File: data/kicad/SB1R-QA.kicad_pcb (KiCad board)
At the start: 4 copper layers, 230 x 228 mm, 5 parts

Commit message: Damping resistors 680 ohm, results, docs and regression for SB1R-Q
- RD1/RD2 value 680 ohm (minimax first gate over Cself 50-200 pF with the
  real AB1T input): 5.1-5.5 us aligned, 7.1-7.5 us at the worst real leak
  (10 mV); gated noise +4 % at 6 us, < 2 % from 20 us. Firmware rule: keep
  BLANK open through turn-off unless the leak exceeds amplifier headroom.
- QB leak after moving its terminals to r23 and re-tuning B (9/9/9/20/6):
  0.07 / 0.59 / 6.0 / 10.3 mV (was 0.005 / 0.85 / 4.4 / 11.0 mV).
- Regenerated SB1R-QA/QB Gerbers and KiCad files, seeds and results;
  sbq_damping.json replaced by sbq_damping2.json; figures SBQ_DAMPING2,
  RX_PLATFORM_QUAD and LEVELS_SCHEMATIC redrawn.
- DESIGN_STATE, CORRECTIONS (5 rows), ASSUMPTIONS (row 14, new row 21),
  OPEN_ITEMS (1 and 12), check counts, stale P01/P02/C04 prompts.
- regress.py: 47 geometry checks, damping fitted, first gate and noise.

Co-Authored-By: Claude Opus 5.5 <noreply@anthropic.com>
Claude-Session: https://claude.ai/code/session_01SK9nuqTzvCJwnmscD6XRZs
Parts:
- added RD1: 680R 0.1% thin film 0805, non-magnetic terminations preferr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, Resistor_SMD:R_0805_2012Metric, F.Cu at (150.0, 87.0)
- added RD2: 680R 0.1% thin film 0805, non-magnetic terminations preferr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, Resistor_SMD:R_0805_2012Metric, F.Cu at (133.9, 103.9)
- added T1: , SB1R:TRANSFER_PAD, F.Cu at (135.8, 101.9)
- added T2: , SB1R:TRANSFER_PAD, F.Cu at (131.9, 105.8)
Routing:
- net QA_COIL: track 16989.1 -> 16995.2 mm
- net QB_COIL: track 0.00 -> 3.64 mm
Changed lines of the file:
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@@
   (net 0 "")
   (net 1 "QA_COIL")
+  (net 2 "QB_COIL")
+  (footprint "SB1R:TRANSFER_PAD" (layer "F.Cu") (at 135.812 101.898) (property "Reference" "T1" (at 0 -2) (layer "F.SilkS")) (pad "1" thru_hole circle (at 0 0) (size 1.6 1.6) (drill 0.8) (layers "*.Cu" "*.Mask") (net 2 "QB_COIL")))
+  (footprint "SB1R:TRANSFER_PAD" (layer "F.Cu") (at 131.898 105.812) (property "Reference" "T2" (at 0 -2) (layer "F.SilkS")) (pad "1" thru_hole circle (at 0 0) (size 1.6 1.6) (drill 0.8) (layers "*.Cu" "*.Mask") (net 2 "QB_COIL")))
+  (footprint "Resistor_SMD:R_0805_2012Metric" (layer "F.Cu") (at 150.000 87.000 180.000) (property "Reference" "RD1" (at 0 -1.6) (layer "F.SilkS")) (property "Value" "680R 0.1% thin film 0805, non-magnetic terminations preferred (unverified)" (at 0 1.6) (layer "F.Fab")) (pad "1" smd roundrect (at -0.95 0 180.000) (size 1.0 1.3) (layers "F.Cu" "F.Paste" "F.Mask") (roundrect_rratio 0.25) (net 1 "QA_COIL")) (pad "2" smd roundrect (at 0.95 0 180.000) (size 1.0 1.3) (layers "F.Cu" "F.Paste" "F.Mask") (roundrect_rratio 0.25) (net 1 "QA_COIL")))
+  (footprint "Resistor_SMD:R_0805_2012Metric" (layer "F.Cu") (at 133.855 103.855 -135.000) (property "Reference" "RD2" (at 0 -1.6) (layer "F.SilkS")) (property "Value" "680R 0.1% thin film 0805, non-magnetic terminations preferred (unverified)" (at 0 1.6) (layer "F.Fab")) (pad "1" smd roundrect (at -0.95 0 -135.000) (size 1.0 1.3) (layers "F.Cu" "F.Paste" "F.Mask") (roundrect_rratio 0.25) (net 2 "QB_COIL")) (pad "2" smd roundrect (at 0.95 0 -135.000) (size 1.0 1.3) (layers "F.Cu" "F.Paste" "F.Mask") (roundrect_rratio 0.25) (net 2 "QB_COIL")))
+  (segment (start 154.0000 87.0000) (end 150.9500 87.0000) (width 0.4) (layer "F.Cu") (net 1))
+  (segment (start 149.0500 87.0000) (end 146.0000 87.0000) (width 0.4) (layer "F.Cu") (net 1))
+  (segment (start 135.8117 101.8977) (end 134.5265 103.1830) (width 0.4) (layer "F.Cu") (net 2))
+  (segment (start 133.1830 104.5265) (end 131.8977 105.8117) (width 0.4) (layer "F.Cu") (net 2))
   (footprint "SB1R:LEAD_PAD" (layer "F.Cu") (at 154.000 87.000) (property "Reference" "P1" (at 0 -2) (layer "F.SilkS")) (pad "1" thru_hole circle (at 0 0) (size 1.6 1.6) (drill 0.8) (layers "*.Cu" "*.Mask") (net 1 "QA_COIL")))
   (footprint "SB1R:LEAD_PAD" (layer "F.Cu") (at 146.000 87.000) (property "Reference" "P2" (at 0 -2) (layer "F.SilkS")) (pad "1" thru_hole circle (at 0 0) (size 1.6 1.6) (drill 0.8) (layers "*.Cu" "*.Mask") (net 1 "QA_COIL")))

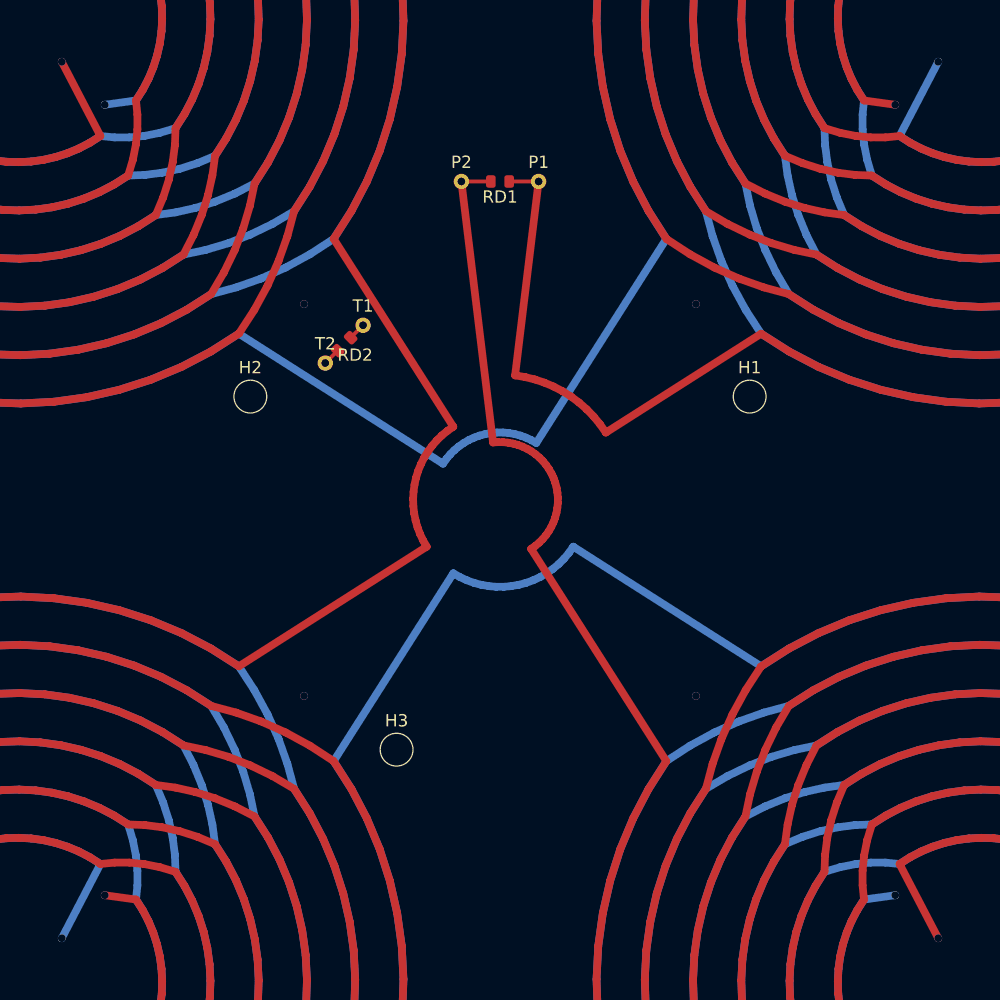
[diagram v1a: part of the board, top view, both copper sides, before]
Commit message: Step 2: CB1D options, SB1R via drill, TXJ1 pads, fab-floor rules, finishes (KiCad 9: 5 boards, 0 errors / 0 unconnected)
- SB1R: via drill 0.4 mm (was 0.8 = no annular ring in the KiCad files and the PTH drill files); QB transfer nets QB_T1/QB_T2; Gerbers SB1R_QA_v2 / SB1R_QB_v2, old marked superseded; sbq sims unchanged (0 numbers moved)
- TXJ1: AWG12 pads 3.8 mm (edge distance 0.6 mm); Gerbers TXJ1_v2
- CB1D: RJB10 0R fitted on JB.10, RJ5/RJ6 DNP grounds for JTR.5/.6 (61 parts, 44/44 nets); Gerbers CB1D_B2; wiring alias JB10_VCM
- dru_gen: conservative Advanced Circuits / TTM floor (UNVERIFIED), SB1R keys; no ENIG near the coil/receivers (immersion silver / HASL); docs/design/FAB_RULES.md
- make kicad-drc covers CB1D, LB1, TXJ1, SB1R-QA/QB; regress 42 pass; CORRECTIONS, DESIGN_STATE, OPEN_ITEMS 23/25-27, ASSUMPTIONS 31

Co-Authored-By: Claude Sonnet 5.5 <noreply@anthropic.com>
Claude-Session: https://claude.ai/code/session_01T7iU5pGiBfkKRBbe2JcTJx
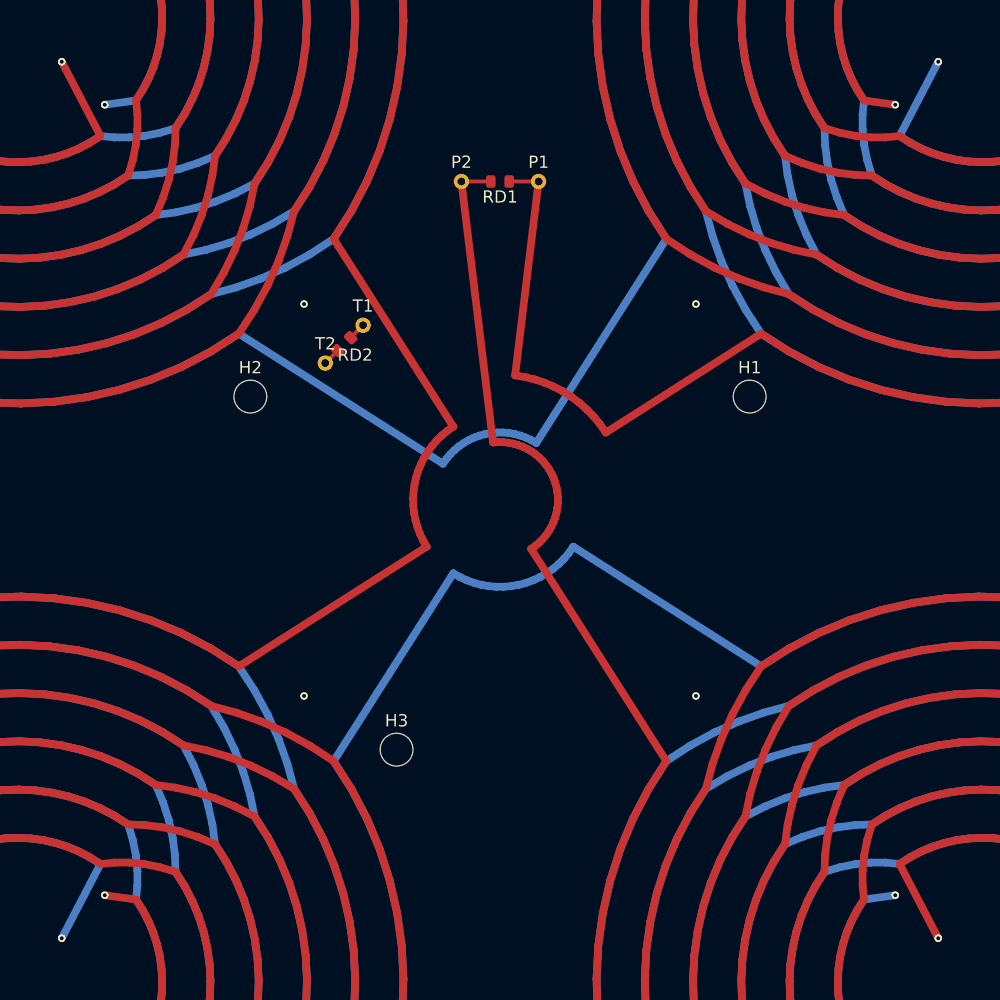
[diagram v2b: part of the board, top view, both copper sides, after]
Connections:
- RD2 pad 1: QB_COIL -> QB_T1
- RD2 pad 2: QB_COIL -> QB_T2
- T1 pad 1: QB_COIL -> QB_T1
- T2 pad 1: QB_COIL -> QB_T2
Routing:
- net QB_COIL: track 3.64 -> 0.00 mm
- net QB_T2: track 0.00 -> 1.82 mm
- net QB_T1: track 0.00 -> 1.82 mm
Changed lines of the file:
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@@
   (paper "A3")
   (layers (0 "F.Cu" signal) (1 "In1.Cu" signal) (2 "In2.Cu" signal) (31 "B.Cu" signal) (34 "B.Paste" user) (35 "F.Paste" user) (36 "B.SilkS" user "B.Silkscreen") (37 "F.SilkS" user "F.Silkscreen") (38 "B.Mask" user) (39 "F.Mask" user) (40 "Dwgs.User" user "User.Drawings") (41 "Cmts.User" user "User.Comments") (44 "Edge.Cuts" user) (47 "F.CrtYd" user "F.Courtyard") (49 "F.Fab" user))
-  (setup (pad_to_mask_clearance 0.05) (stackup (layer "F.Cu" (type "copper") (thickness 0.035)) (layer "dielectric 1" (type "prepreg") (thickness 0.15)) (layer "In1.Cu" (type "copper") (thickness 0.035)) (layer "dielectric 2" (type "core") (thickness 0.34)) (layer "In2.Cu" (type "copper") (thickness 0.035)) (layer "dielectric 3" (type "prepreg") (thickness 0.15)) (layer "B.Cu" (type "copper") (thickness 0.035)) (copper_finish "ENIG")))
+  (setup (pad_to_mask_clearance 0.05) (stackup (layer "F.Cu" (type "copper") (thickness 0.035)) (layer "dielectric 1" (type "prepreg") (thickness 0.15)) (layer "In1.Cu" (type "copper") (thickness 0.035)) (layer "dielectric 2" (type "core") (thickness 0.34)) (layer "In2.Cu" (type "copper") (thickness 0.035)) (layer "dielectric 3" (type "prepreg") (thickness 0.15)) (layer "B.Cu" (type "copper") (thickness 0.035)) (copper_finish "Immersion silver")))
   (net 0 "")
   (net 1 "QA_COIL")
-  (net 2 "QB_COIL")
-  (footprint "SB1R:TRANSFER_PAD" (layer "F.Cu") (at 135.812 101.898) (property "Reference" "T1" (at 0 -2) (layer "F.SilkS")) (pad "1" thru_hole circle (at 0 0) (size 1.6 1.6) (drill 0.8) (layers "*.Cu" "*.Mask") (net 2 "QB_COIL")))
-  (footprint "SB1R:TRANSFER_PAD" (layer "F.Cu") (at 131.898 105.812) (property "Reference" "T2" (at 0 -2) (layer "F.SilkS")) (pad "1" thru_hole circle (at 0 0) (size 1.6 1.6) (drill 0.8) (layers "*.Cu" "*.Mask") (net 2 "QB_COIL")))
+  (net 2 "QB_T1")
+  (net 3 "QB_T2")
+  (footprint "SB1R:TRANSFER_PAD" (layer "F.Cu") (at 135.812 101.898) (property "Reference" "T1" (at 0 -2) (layer "F.SilkS")) (pad "1" thru_hole circle (at 0 0) (size 1.6 1.6) (drill 0.8) (layers "*.Cu" "*.Mask") (net 2 "QB_T1")))
+  (footprint "SB1R:TRANSFER_PAD" (layer "F.Cu") (at 131.898 105.812) (property "Reference" "T2" (at 0 -2) (layer "F.SilkS")) (pad "1" thru_hole circle (at 0 0) (size 1.6 1.6) (drill 0.8) (layers "*.Cu" "*.Mask") (net 3 "QB_T2")))
   (footprint "Resistor_SMD:R_0805_2012Metric" (layer "F.Cu") (at 150.000 87.000 180.000) (property "Reference" "RD1" (at 0 -1.6) (layer "F.SilkS")) (property "Value" "680R 0.1% thin film 0805, non-magnetic terminations preferred (unverified)" (at 0 1.6) (layer "F.Fab")) (pad "1" smd roundrect (at -0.95 0 180.000) (size 1.0 1.3) (layers "F.Cu" "F.Paste" "F.Mask") (roundrect_rratio 0.25) (net 1 "QA_COIL")) (pad "2" smd roundrect (at 0.95 0 180.000) (size 1.0 1.3) (layers "F.Cu" "F.Paste" "F.Mask") (roundrect_rratio 0.25) (net 1 "QA_COIL")))
-  (footprint "Resistor_SMD:R_0805_2012Metric" (layer "F.Cu") (at 133.855 103.855 -135.000) (property "Reference" "RD2" (at 0 -1.6) (layer "F.SilkS")) (property "Value" "680R 0.1% thin film 0805, non-magnetic terminations preferred (unverified)" (at 0 1.6) (layer "F.Fab")) (pad "1" smd roundrect (at -0.95 0 -135.000) (size 1.0 1.3) (layers "F.Cu" "F.Paste" "F.Mask") (roundrect_rratio 0.25) (net 2 "QB_COIL")) (pad "2" smd roundrect (at 0.95 0 -135.000) (size 1.0 1.3) (layers "F.Cu" "F.Paste" "F.Mask") (roundrect_rratio 0.25) (net 2 "QB_COIL")))
+  (footprint "Resistor_SMD:R_0805_2012Metric" (layer "F.Cu") (at 133.855 103.855 -135.000) (property "Reference" "RD2" (at 0 -1.6) (layer "F.SilkS")) (property "Value" "680R 0.1% thin film 0805, non-magnetic terminations preferred (unverified)" (at 0 1.6) (layer "F.Fab")) (pad "1" smd roundrect (at -0.95 0 -135.000) (size 1.0 1.3) (layers "F.Cu" "F.Paste" "F.Mask") (roundrect_rratio 0.25) (net 2 "QB_T1")) (pad "2" smd roundrect (at 0.95 0 -135.000) (size 1.0 1.3) (layers "F.Cu" "F.Paste" "F.Mask") (roundrect_rratio 0.25) (net 3 "QB_T2")))
   (segment (start 154.0000 87.0000) (end 150.9500 87.0000) (width 0.4) (layer "F.Cu") (net 1))
   (segment (start 149.0500 87.0000) (end 146.0000 87.0000) (width 0.4) (layer "F.Cu") (net 1))
   (segment (start 135.8117 101.8977) (end 134.5265 103.1830) (width 0.4) (layer "F.Cu") (net 2))
-  (segment (start 133.1830 104.5265) (end 131.8977 105.8117) (width 0.4) (layer "F.Cu") (net 2))
+  (segment (start 133.1830 104.5265) (end 131.8977 105.8117) (width 0.4) (layer "F.Cu") (net 3))
   (footprint "SB1R:LEAD_PAD" (layer "F.Cu") (at 154.000 87.000) (property "Reference" "P1" (at 0 -2) (layer "F.SilkS")) (pad "1" thru_hole circle (at 0 0) (size 1.6 1.6) (drill 0.8) (layers "*.Cu" "*.Mask") (net 1 "QA_COIL")))
   (footprint "SB1R:LEAD_PAD" (layer "F.Cu") (at 146.000 87.000) (property "Reference" "P2" (at 0 -2) (layer "F.SilkS")) (pad "1" thru_hole circle (at 0 0) (size 1.6 1.6) (drill 0.8) (layers "*.Cu" "*.Mask") (net 1 "QA_COIL")))
@@
   (segment (start 157.1406 125.4782) (end 157.5909 124.8350) (width 0.8) (layer "B.Cu") (net 1))
   (segment (start 157.5909 124.8350) (end 177.0569 137.2339) (width 0.8) (layer "B.Cu") (net 1))
-  (via (at 190.9490 79.0510) (size 0.8) (drill 0.8) (layers "F.Cu" "B.Cu") (net 1))
-  (via (at 170.3015 99.6985) (size 0.8) (drill 0.8) (layers "F.Cu" "B.Cu") (net 1))
-  (via (at 195.4038 74.5962) (size 0.8) (drill 0.8) (layers "F.Cu" "B.Cu") (net 1))
-  (via (at 109.0510 79.0510) (size 0.8) (drill 0.8) (layers "F.Cu" "B.Cu") (net 1))
-  (via (at 129.6985 99.6985) (size 0.8) (drill 0.8) (layers "F.Cu" "B.Cu") (net 1))
-  (via (at 104.5962 74.5962) (size 0.8) (drill 0.8) (layers "F.Cu" "B.Cu") (net 1))
-  (via (at 109.0510 160.9490) (size 0.8) (drill 0.8) (layers "F.Cu" "B.Cu") (net 1))
-  (via (at 129.6985 140.3015) (size 0.8) (drill 0.8) (layers "F.Cu" "B.Cu") (net 1))
-  (via (at 104.5962 165.4038) (size 0.8) (drill 0.8) (layers "F.Cu" "B.Cu") (net 1))
-  (via (at 190.9490 160.9490) (size 0.8) (drill 0.8) (layers "F.Cu" "B.Cu") (net 1))
-  (via (at 170.3015 140.3015) (size 0.8) (drill 0.8) (layers "F.Cu" "B.Cu") (net 1))
-  (via (at 195.4038 165.4038) (size 0.8) (drill 0.8) (layers "F.Cu" "B.Cu") (net 1))
+  (via (at 190.9490 79.0510) (size 0.8) (drill 0.4) (layers "F.Cu" "B.Cu") (net 1))
+  (via (at 170.3015 99.6985) (size 0.8) (drill 0.4) (layers "F.Cu" "B.Cu") (net 1))
+  (via (at 195.4038 74.5962) (size 0.8) (drill 0.4) (layers "F.Cu" "B.Cu") (net 1))
+  (via (at 109.0510 79.0510) (size 0.8) (drill 0.4) (layers "F.Cu" "B.Cu") (net 1))
+  (via (at 129.6985 99.6985) (size 0.8) (drill 0.4) (layers "F.Cu" "B.Cu") (net 1))
+  (via (at 104.5962 74.5962) (size 0.8) (drill 0.4) (layers "F.Cu" "B.Cu") (net 1))
+  (via (at 109.0510 160.9490) (size 0.8) (drill 0.4) (layers "F.Cu" "B.Cu") (net 1))
+  (via (at 129.6985 140.3015) (size 0.8) (drill 0.4) (layers "F.Cu" "B.Cu") (net 1))
+  (via (at 104.5962 165.4038) (size 0.8) (drill 0.4) (layers "F.Cu" "B.Cu") (net 1))
+  (via (at 190.9490 160.9490) (size 0.8) (drill 0.4) (layers "F.Cu" "B.Cu") (net 1))
+  (via (at 170.3015 140.3015) (size 0.8) (drill 0.4) (layers "F.Cu" "B.Cu") (net 1))
+  (via (at 195.4038 165.4038) (size 0.8) (drill 0.4) (layers "F.Cu" "B.Cu") (net 1))
   (gr_line (start 263.982 118.000) (end 263.930 116.017) (stroke (width 0.1) (type default)) (layer "Edge.Cuts"))
   (gr_line (start 263.930 116.017) (end 263.844 114.034) (stroke (width 0.1) (type default)) (layer "Edge.Cuts"))
